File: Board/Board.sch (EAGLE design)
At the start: 55 parts, among them IC1 NJM4556, J1 POWER_JACKPTH, K1 351, X1 RCA-4-117-01

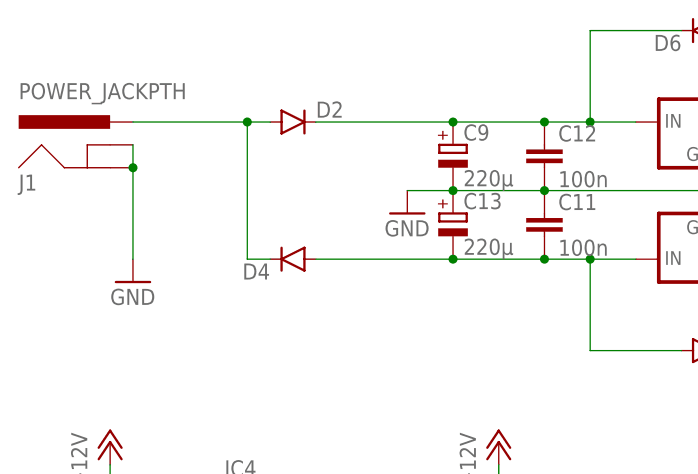
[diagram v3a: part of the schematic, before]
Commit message: added beefier rectifier diodes
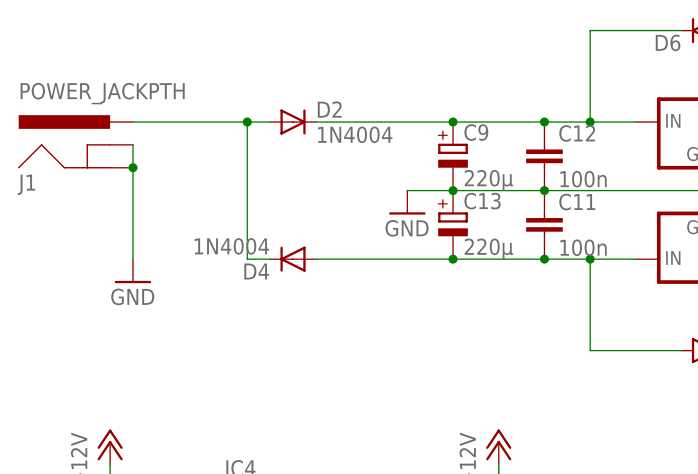
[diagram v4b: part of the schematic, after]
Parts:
- D2, D4: value (none) -> 1N4004; device SparkFun-DiscreteSemi:DIODEBAS16 -> diode:1N4004
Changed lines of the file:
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@@
 <part name="GND6" library="supply1" library_urn="urn:adsk.eagle:library:371" deviceset="GND" device=""/>
 <part name="J1" library="SparkFun-Connectors" deviceset="POWER_JACK" device="PTH"/>
-<part name="D2" library="SparkFun-DiscreteSemi" deviceset="DIODE" device="BAS16"/>
-<part name="D4" library="SparkFun-DiscreteSemi" deviceset="DIODE" device="BAS16"/>
+<part name="D2" library="diode" library_urn="urn:adsk.eagle:library:210" deviceset="1N4004" device="" package3d_urn="urn:adsk.eagle:package:43336/1"/>
+<part name="D4" library="diode" library_urn="urn:adsk.eagle:library:210" deviceset="1N4004" device="" package3d_urn="urn:adsk.eagle:package:43336/1"/>
 <part name="C2" library="rcl" library_urn="urn:adsk.eagle:library:334" deviceset="C-EU" device="C0603" package3d_urn="urn:adsk.eagle:package:23616/2" value="100n"/>
 <part name="C8" library="rcl" library_urn="urn:adsk.eagle:library:334" deviceset="C-EU" device="C0603" package3d_urn="urn:adsk.eagle:package:23616/2" value="100n"/>
@@
 <instance part="GND6" gate="1" x="147.32" y="58.42"/>
 <instance part="J1" gate="G$1" x="-5.08" y="160.02"/>
-<instance part="D2" gate="G$1" x="15.24" y="167.64"/>
-<instance part="D4" gate="G$1" x="15.24" y="152.4" rot="R180"/>
+<instance part="D2" gate="1" x="15.24" y="167.64"/>
+<instance part="D4" gate="1" x="15.24" y="152.4" rot="R180"/>
 <instance part="C2" gate="G$1" x="73.66" y="165.1"/>
 <instance part="C8" gate="G$1" x="73.66" y="157.48"/>
@@
 <segment>
 <pinref part="J1" gate="G$1" pin="PWR"/>
-<pinref part="D2" gate="G$1" pin="A"/>
+<pinref part="D2" gate="1" pin="A"/>
 <wire x1="-2.54" y1="167.64" x2="10.16" y2="167.64" width="0.1524" layer="91"/>
 <wire x1="10.16" y1="167.64" x2="12.7" y2="167.64" width="0.1524" layer="91"/>
-<pinref part="D4" gate="G$1" pin="C"/>
+<pinref part="D4" gate="1" pin="C"/>
 <wire x1="12.7" y1="152.4" x2="10.16" y2="152.4" width="0.1524" layer="91"/>
 <wire x1="10.16" y1="152.4" x2="10.16" y2="167.64" width="0.1524" layer="91"/>
@@
 <net name="N$23" class="0">
 <segment>
-<pinref part="D4" gate="G$1" pin="A"/>
+<pinref part="D4" gate="1" pin="A"/>
 <wire x1="17.78" y1="152.4" x2="33.02" y2="152.4" width="0.1524" layer="91"/>
 <pinref part="C11" gate="G$1" pin="2"/>
@@
 <net name="N$24" class="0">
 <segment>
-<pinref part="D2" gate="G$1" pin="C"/>
+<pinref part="D2" gate="1" pin="C"/>
 <wire x1="17.78" y1="167.64" x2="33.02" y2="167.64" width="0.1524" layer="91"/>
 <pinref part="C12" gate="G$1" pin="1"/>
